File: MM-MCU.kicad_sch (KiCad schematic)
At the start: 17 parts, among them U5 STM32F205RGTx

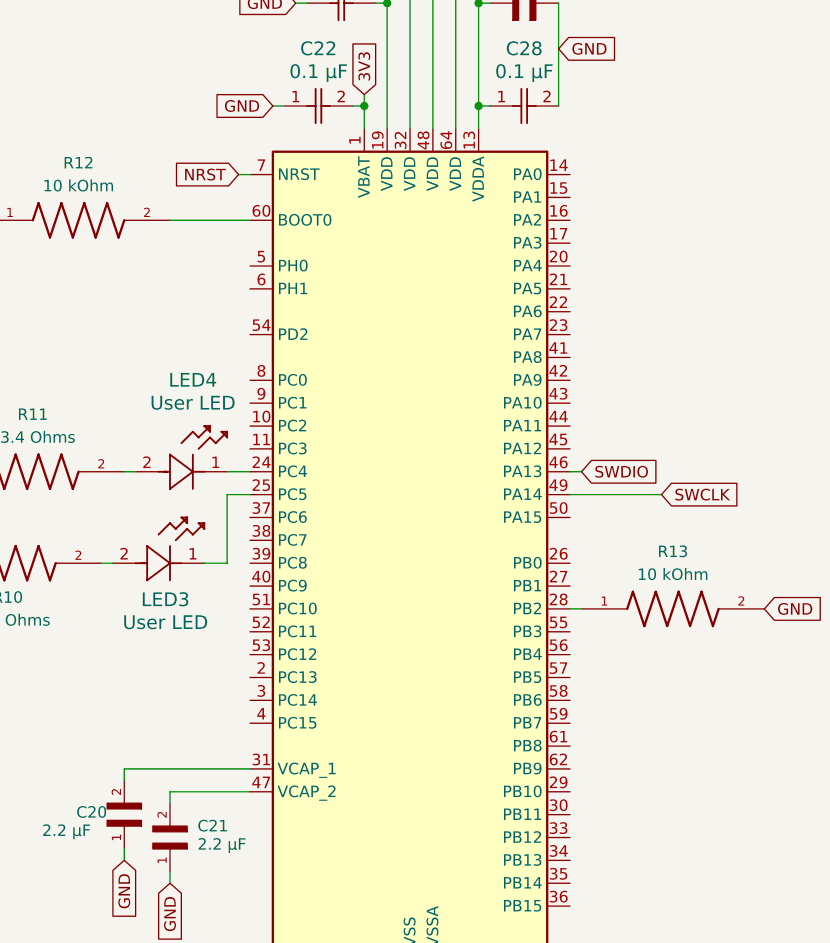
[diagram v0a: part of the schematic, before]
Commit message: added power switch
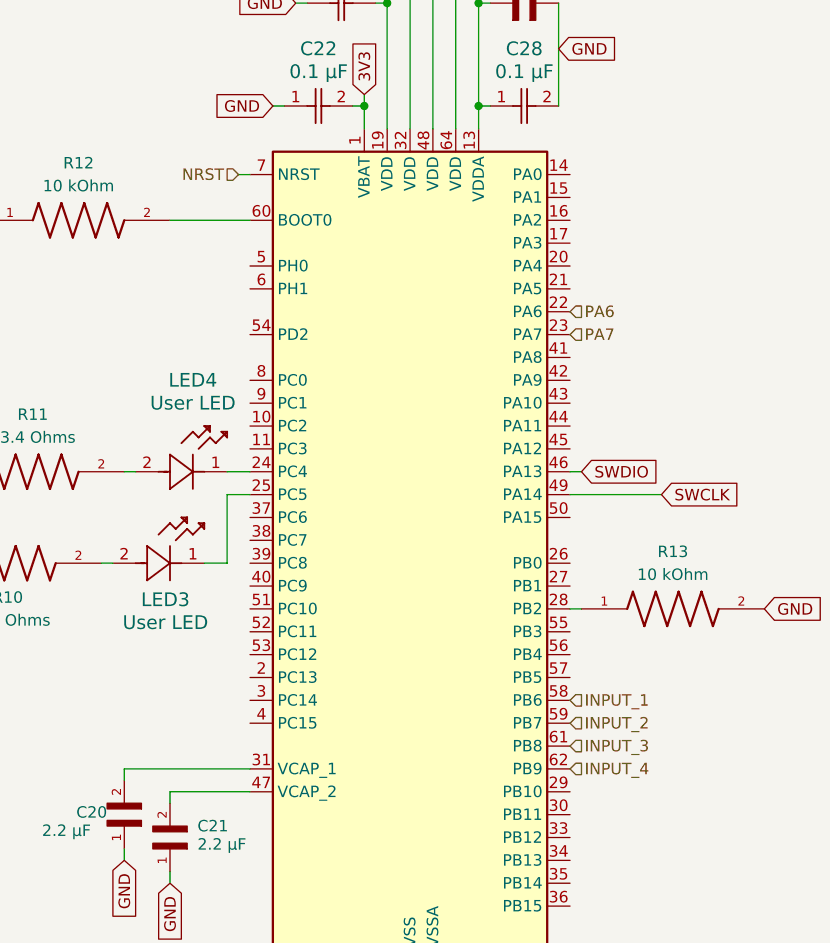
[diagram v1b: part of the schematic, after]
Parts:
- LED3, LED4: footprint LED_LTL-4231N_LTO -> (none)
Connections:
- net PA6: now reaches U5.22 (PA6)
- net PA7: now reaches U5.23 (PA7)
- net INPUT_1: now reaches U5.58 (PB6)
- net INPUT_2: now reaches U5.59 (PB7)
- net INPUT_3: now reaches U5.61 (PB8)
- net INPUT_4: now reaches U5.62 (PB9)
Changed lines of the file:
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@@
-		)
-	)
-	(global_label "NRST"
-		(shape input)
-		(at 90.17 87.63 180)
-		(fields_autoplaced yes)
-		(effects
-			(font
-				(size 1.27 1.27)
-			)
-			(justify right)
-		)
-		(property "Intersheetrefs" "${INTERSHEET_REFS}"
-			(at 82.4072 87.63 0)
-			(effects
-				(font
-					(size 1.27 1.27)
-				)
-				(justify right)
-				(hide yes)
-			)
 		)
 	)
@@
 				(hide yes)
 			)
+		)
+	)
+	(hierarchical_label "INPUT_2"
+		(shape input)
+		(at 127 148.59 0)
+		(effects
+			(font
+				(size 1.27 1.27)
+			)
+			(justify left)
+		)
+	)
+	(hierarchical_label "NRST"
+		(shape input)
+		(at 90.17 87.63 180)
+		(effects
+			(font
+				(size 1.27 1.27)
+			)
+			(justify right)
+		)
+	)
+	(hierarchical_label "PA6"
+		(shape input)
+		(at 127 102.87 0)
+		(effects
+			(font
+				(size 1.27 1.27)
+			)
+			(justify left)
+		)
+	)
+	(hierarchical_label "INPUT_1"
+		(shape input)
+		(at 127 146.05 0)
+		(effects
+			(font
+				(size 1.27 1.27)
+			)
+			(justify left)
+		)
+	)
+	(hierarchical_label "INPUT_3"
+		(shape input)
+		(at 127 151.13 0)
+		(effects
+			(font
+				(size 1.27 1.27)
+			)
+			(justify left)
+		)
+	)
+	(hierarchical_label "PA7"
+		(shape input)
+		(at 127 105.41 0)
+		(effects
+			(font
+				(size 1.27 1.27)
+			)
+			(justify left)
+		)
+	)
+	(hierarchical_label "INPUT_4"
+		(shape input)
+		(at 127 153.67 0)
+		(effects
+			(font
+				(size 1.27 1.27)
+			)
+			(justify left)
 		)
 	)
@@
 			)
 		)
-		(property "Footprint" "LED_LTL-4231N_LTO"
+		(property "Footprint" ""
 			(at 76.2 130.81 0)
 			(effects
@@
 			)
 		)
-		(property "Footprint" "LED_LTL-4231N_LTO"
+		(property "Footprint" ""
 			(at 78.74 120.65 0)
 			(effects

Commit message: fixedled orignetation and linked to ground + duplicated IR emitter/receiver pairs
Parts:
- C22, C23, C24, C26, C27, C28: footprint 0.1µFCapacitor_footprints:CAP_0402_N_WAL-L -> Ceramic_Capacitor_0.1uF_CL21B104KBCNNNC:CAPC2012X95N
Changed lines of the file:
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@@
 			)
 		)
-		(property "Footprint" "0.1µFCapacitor_footprints:CAP_0402_N_WAL-L"
+		(property "Footprint" "Ceramic_Capacitor_0.1uF_CL21B104KBCNNNC:CAPC2012X95N"
 			(at 95.25 80.01 0)
 			(effects
@@
 			)
 		)
-		(property "Footprint" "0.1µFCapacitor_footprints:CAP_0402_N_WAL-L"
+		(property "Footprint" "Ceramic_Capacitor_0.1uF_CL21B104KBCNNNC:CAPC2012X95N"
 			(at 97.79 68.58 0)
 			(effects
@@
 			)
 		)
-		(property "Footprint" "0.1µFCapacitor_footprints:CAP_0402_N_WAL-L"
+		(property "Footprint" "Ceramic_Capacitor_0.1uF_CL21B104KBCNNNC:CAPC2012X95N"
 			(at 102.87 38.1 0)
 			(effects
@@
 			)
 		)
-		(property "Footprint" "0.1µFCapacitor_footprints:CAP_0402_N_WAL-L"
+		(property "Footprint" "Ceramic_Capacitor_0.1uF_CL21B104KBCNNNC:CAPC2012X95N"
 			(at 100.33 48.26 0)
 			(effects
@@
 			)
 		)
-		(property "Footprint" "0.1µFCapacitor_footprints:CAP_0402_N_WAL-L"
+		(property "Footprint" "Ceramic_Capacitor_0.1uF_CL21B104KBCNNNC:CAPC2012X95N"
 			(at 118.11 80.01 0)
 			(effects
@@
 			)
 		)
-		(property "Footprint" "0.1µFCapacitor_footprints:CAP_0402_N_WAL-L"
+		(property "Footprint" "Ceramic_Capacitor_0.1uF_CL21B104KBCNNNC:CAPC2012X95N"
 			(at 105.41 27.94 0)
 			(effects

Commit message: Add files via upload
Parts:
- removed C22, C23, C24, C26, C27, C28: 0.1 µF, Ceramic_Capacitor_0.1uF_CL21B104KBCNNNC:CAPC2012X95N, symbol 0.1µFCapacitor_2025-12-15_19-47-12:0402B104K160CT
- added C1, C2, C3, C4, C5, C6: 0.1 µF, CL05A104KA5NNNC:CAPC1005X55N, symbol 0.1µFCapacitor_CL05A104KA5NNNC:CL05A104KA5NNNC
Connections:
- net 3V3: now also C1.1, C2.2, C3.2, C4.2, C5.2, C6.2
- net GND: now also C1.2, C2.1, C3.1, C4.1, C5.1, C6.1

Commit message: Add files via upload
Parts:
- removed R10, R11: 23.4 Ohms, RN73R1JTTD23R4B25:RESC1608X55N, symbol 23.4ohmResistor_RN73R1JTTD23R4B25:RN73R1JTTD23R4B25
- added R1, R2: 60.4 Ohms, CR0603-FX-60R4ELF:RESC1608X55N, symbol 60.4ohmResistor_CR0603-FX-60R4ELF:CR0603-FX-60R4ELF
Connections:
- net 3V3: now also R1.1, R2.1
- net at LED3.2: now also R2.2
- net at LED4.2: now also R1.2
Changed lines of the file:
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@@
-	)
-	(symbol
-		(lib_id "23.4ohmResistor_RN73R1JTTD23R4B25:RN73R1JTTD23R4B25")
-		(at 67.31 120.65 0)
-		(unit 1)
-		(exclude_from_sim no)
-		(in_bom yes)
-		(on_board yes)
-		(dnp no)
-		(fields_autoplaced yes)
-		(property "Reference" "R11"
-			(at 67.31 114.3 0)
-			(effects
-				(font
-					(size 1.27 1.27)
-				)
-			)
-		)
-		(property "Value" "23.4 Ohms"
-			(at 67.31 116.84 0)
-			(effects
-				(font
-					(size 1.27 1.27)
-				)
-			)
-		)
-		(property "Footprint" "RN73R1JTTD23R4B25:RESC1608X55N"
-			(at 67.31 120.65 0)
-			(effects
-				(font
-					(size 1.27 1.27)
-				)
-				(justify bottom)
-				(hide yes)
-			)
-		)
-		(property "Datasheet" ""
-			(at 67.31 120.65 0)
-			(effects
-				(font
-					(size 1.27 1.27)
-				)
-				(hide yes)
-			)
-		)
-		(property "Description" ""
-			(at 67.31 120.65 0)
-			(effects
-				(font
-					(size 1.27 1.27)
-				)
-				(hide yes)
-			)
-		)
-		(pin "1"
-		)
-		(pin "2"
-		)
-		(instances
-			(project "IREmitter"
-				(path "/d311851a-8b0b-4acf-b2e7-1b968b2adbe7/2e1dc814-2c57-413c-a832-0cf6350c5f62"
-					(reference "R11")
-					(unit 1)
-				)
-			)
-		)
-	)
-	(symbol
-		(lib_id "23.4ohmResistor_RN73R1JTTD23R4B25:RN73R1JTTD23R4B25")
-		(at 64.77 130.81 0)
-		(unit 1)
-		(exclude_from_sim no)
-		(in_bom yes)
-		(on_board yes)
-		(dnp no)
-		(property "Reference" "R10"
-			(at 64.516 134.62 0)
-			(effects
-				(font
-					(size 1.27 1.27)
-				)
-			)
-		)
-		(property "Value" "23.4 Ohms"
-			(at 64.516 137.16 0)
-			(effects
-				(font
-					(size 1.27 1.27)
-				)
-			)
-		)
-		(property "Footprint" "RN73R1JTTD23R4B25:RESC1608X55N"
-			(at 64.77 130.81 0)
-			(effects
-				(font
-					(size 1.27 1.27)
-				)
-				(justify bottom)
-				(hide yes)
-			)
-		)
-		(property "Datasheet" ""
-			(at 64.77 130.81 0)
-			(effects
-				(font
-					(size 1.27 1.27)
-				)
-				(hide yes)
-			)
-		)
-		(property "Description" ""
-			(at 64.77 130.81 0)
-			(effects
-				(font
-					(size 1.27 1.27)
-				)
-				(hide yes)
-			)
-		)
-		(pin "1"
-		)
-		(pin "2"
-		)
-		(instances
-			(project "IREmitter"
-				(path "/d311851a-8b0b-4acf-b2e7-1b968b2adbe7/2e1dc814-2c57-413c-a832-0cf6350c5f62"
-					(reference "R10")
-					(unit 1)
-				)
-			)
-		)
 	)
 	(symbol
@@
 	)
 	(symbol
+		(lib_id "60.4ohmResistor_CR0603-FX-60R4ELF:CR0603-FX-60R4ELF")
+		(at 67.31 120.65 0)
+		(unit 1)
+		(exclude_from_sim no)
+		(in_bom yes)
+		(on_board yes)
+		(dnp no)
+		(fields_autoplaced yes)
+		(property "Reference" "R1"
+			(at 67.31 114.3 0)
+			(effects
+				(font
+					(size 1.27 1.27)
+				)
+			)
+		)
+		(property "Value" "60.4 Ohms"
+			(at 67.31 116.84 0)
+			(effects
+				(font
+					(size 1.27 1.27)
+				)
+			)
+		)
+		(property "Footprint" "CR0603-FX-60R4ELF:RESC1608X55N"
+			(at 67.31 120.65 0)
+			(effects
+				(font
+					(size 1.27 1.27)
+				)
+				(justify bottom)
+				(hide yes)
+			)
+		)
+		(property "Datasheet" ""
+			(at 67.31 120.65 0)
+			(effects
+				(font
+					(size 1.27 1.27)
+				)
+				(hide yes)
+			)
+		)
+		(property "Description" ""
+			(at 67.31 120.65 0)
+			(effects
+				(font
+					(size 1.27 1.27)
+				)
+				(hide yes)
+			)
+		)
+		(pin "1"
+		)
+		(pin "2"
+		)
+		(instances
+			(project ""
+				(path "/d311851a-8b0b-4acf-b2e7-1b968b2adbe7/2e1dc814-2c57-413c-a832-0cf6350c5f62"
+					(reference "R1")
+					(unit 1)
+				)
+			)
+		)
+	)
+	(symbol
 		(lib_id "0.1µFCapacitor_CL05A104KA5NNNC:CL05A104KA5NNNC")
 		(at 100.33 68.58 0)
@@
 					(unit 1)
 				)
+			)
+		)
+	)
+	(symbol
+		(lib_id "60.4ohmResistor_CR0603-FX-60R4ELF:CR0603-FX-60R4ELF")
+		(at 64.77 130.81 0)
+		(unit 1)
+		(exclude_from_sim no)
+		(in_bom yes)
+		(on_board yes)
+		(dnp no)
+		(fields_autoplaced yes)
+		(property "Reference" "R2"
+			(at 64.77 124.46 0)
+			(effects
+				(font
+					(size 1.27 1.27)
+				)
+			)
+		)
+		(property "Value" "60.4 Ohms"
+			(at 64.77 127 0)
+			(effects
+				(font
+					(size 1.27 1.27)
+				)
+			)
+		)
+		(property "Footprint" "CR0603-FX-60R4ELF:RESC1608X55N"
+			(at 64.77 130.81 0)
+			(effects
+				(font
+					(size 1.27 1.27)
+				)
+				(justify bottom)
+				(hide yes)
+			)
+		)
+		(property "Datasheet" ""
+			(at 64.77 130.81 0)
+			(effects
+				(font
+					(size 1.27 1.27)
+				)
+				(hide yes)
+			)
+		)
+		(property "Description" ""
+			(at 64.77 130.81 0)
+			(effects
+				(font
+					(size 1.27 1.27)
+				)
+				(hide yes)
+			)
+		)
+		(pin "1"
+		)
+		(pin "2"
+		)
+		(instances
+			(project "IREmitter"
+				(path "/d311851a-8b0b-4acf-b2e7-1b968b2adbe7/2e1dc814-2c57-413c-a832-0cf6350c5f62"
+					(reference "R2")
+					(unit 1)
+				)

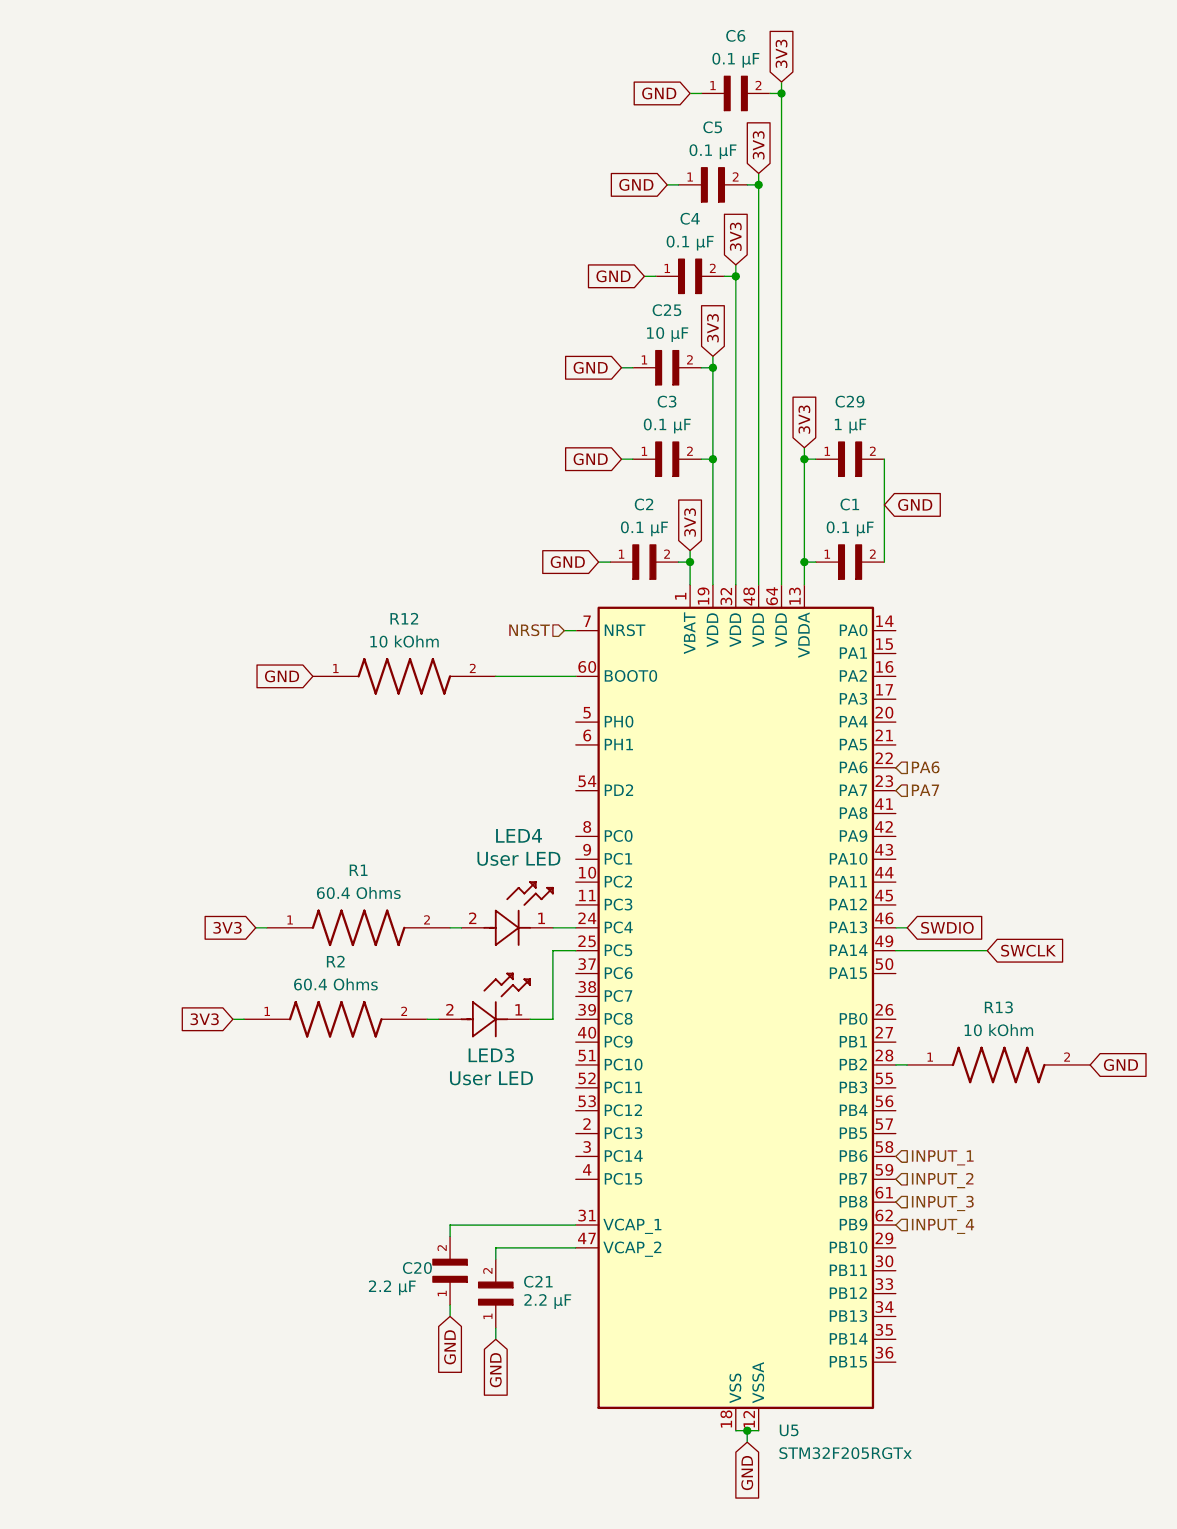
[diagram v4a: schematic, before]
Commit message: redid the 4 emitters receivers, fixed orientation of LEDS and going to continue adding footprints and replace the 60ohm resistors with 300ohm ones
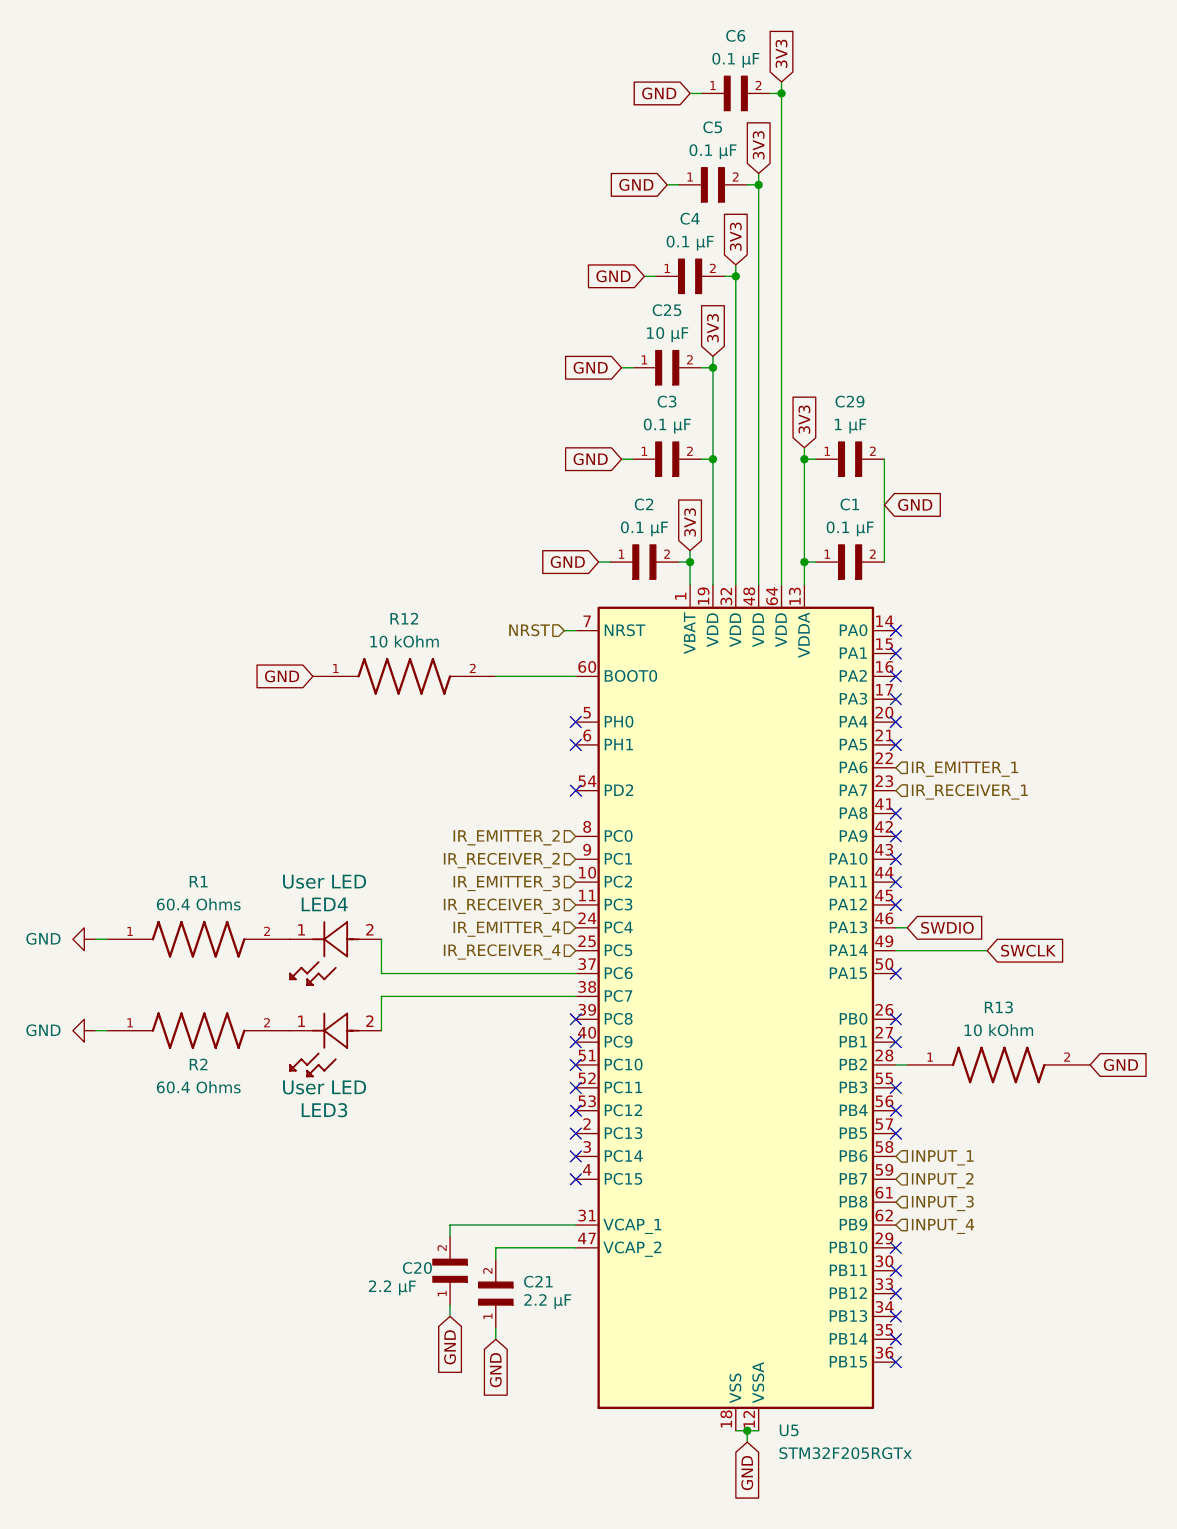
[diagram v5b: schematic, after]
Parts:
- C1, C2, C3, C4, C5, C6: footprint CL05A104KA5NNNC:CAPC1005X55N -> Ceramic_Capacitor_0.1uF_CL21B104KBCNNNC:CAPC2012X95N
- C25: footprint CL21B106KOQNNNE:CAPC2012X140N -> Ceramic_Capacitor_10uF_GRM21BC81C106KA73L:CAPC2012X140N
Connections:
- net 3V3: no longer R1.1, R2.1
- net GND: now also R1.1, R2.1
- net at LED3.1: now also R2.2; no longer U5.25 (PC5)
- net at LED3.2: now also U5.38 (PC7); no longer R2.2
- net at R1.2: now also LED4.1; no longer LED4.2
- net IR_EMITTER_4: now reaches U5.24 (PC4)
- net IR_EMITTER_4: no longer LED4.1
- net IR_EMITTER_3: now reaches U5.10 (PC2)
- net IR_RECEIVER_3: now reaches U5.11 (PC3)
- net at U5.37 (PC6): now also LED4.2
- net IR_EMITTER_2: now reaches U5.8 (PC0)
- net IR_RECEIVER_2: now reaches U5.9 (PC1)
- net PA6 renamed IR_EMITTER_1
- net PA7 renamed IR_RECEIVER_1
- new net IR_RECEIVER_4: U5.25 (PC5)
- no-connect marks 0 -> 34
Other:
- moved on the sheet: LED3, LED4, R1, R2

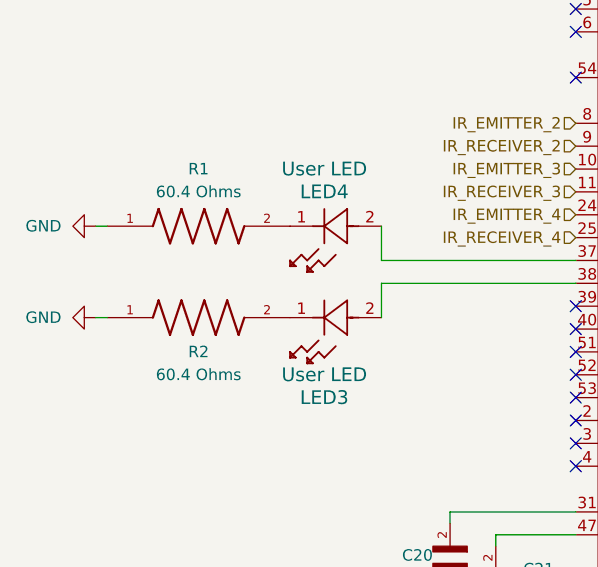
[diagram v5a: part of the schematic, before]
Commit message: finished adding rest of footprints, tried replacing mosfets with no success
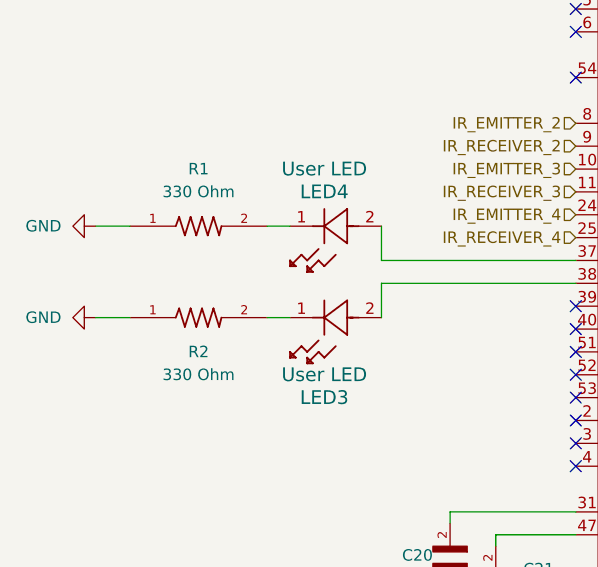
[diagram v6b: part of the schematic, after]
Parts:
- removed R1, R2: 60.4 Ohms, CR0603-FX-60R4ELF:RESC1608X55N, symbol 60.4ohmResistor_CR0603-FX-60R4ELF:CR0603-FX-60R4ELF
- added R1, R2: 330 Ohm, 330_ohm_RC0603FR-07330RL:RESC1607X60N, symbol 330_ohm_RC0603FR-07330RL:RC0603FR-07330RL
- C20, C21: footprint CL10B225KP8NNNC:CAPC1608X90N -> 2.2uF_CL21A226MPQNNNE:CAPC2012X140N
- C29: footprint CL10B105KP8NNNC:CAPC1608X90N -> 1uF_CL10B105KP8NNNC:CAPC1608X90N
- R12, R13: footprint RMCF0805FT10K0:RESC2012X65N -> 10_kohm_RMCF0805FT10K0:RESC2012X65N
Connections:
- net GND: now also R1.1, R2.1
- net at LED3.1: now also R2.2
- net at LED4.1: now also R1.2
